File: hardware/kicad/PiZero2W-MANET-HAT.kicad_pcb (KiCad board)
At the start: 2 copper layers, 65 x 30 mm, 4 parts

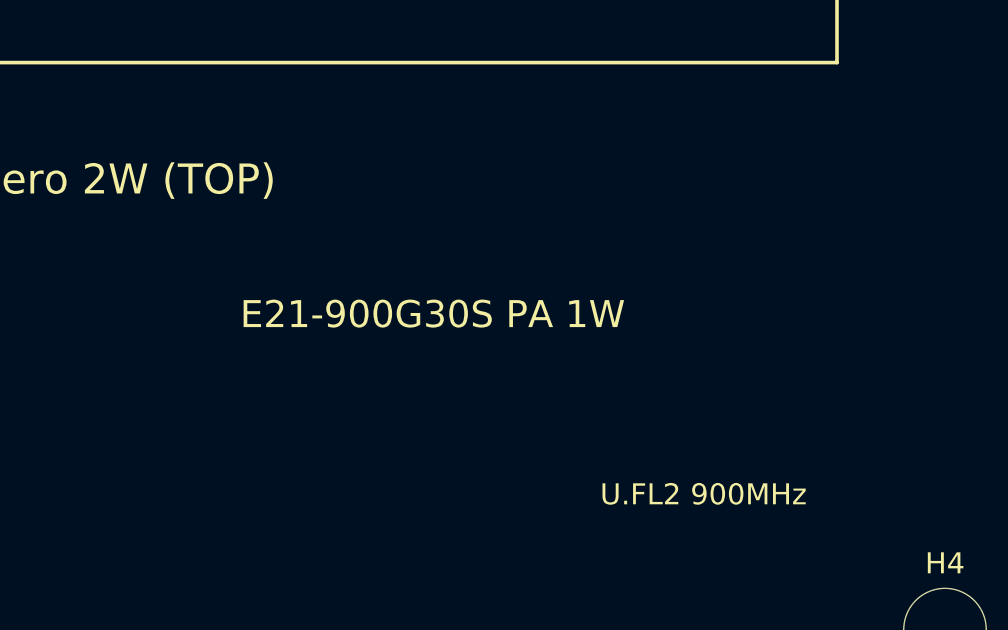
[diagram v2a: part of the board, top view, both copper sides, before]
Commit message: Make E21 PA a DNP/optional Variant B; default to module-only
Deployment is ground/handheld/vehicle (NLOS), where the E21's +3 dB buys
only ~20% range (LINK_BUDGET) against ~620 mA + heat + recert + RX-rate
risk. So restructure as one PCB with two BOM builds:

- Variant A (DEFAULT): module-only ~27 dBm via OpenMANET BCF. E21,
  buck-boost (VPA), LPF and drive pad are DNP; an RF bypass (C_BYP)
  carries the module ANT straight to U.FL #2. Low power (~0.35 A), good
  for battery handhelds, stays on the module's modular cert.
- Variant B (OPTIONAL): populate E21 + VPA + LPF + T/R for +30 dBm
  extended range (fixed/elevated LoS); remove C_BYP; needs custom-BCF
  FEM GPIO control + end-product recert. No respin required.

Updated DECISIONS (B5/B10 resolved + new §C variants & order), SCHEMATIC,
POWER (default-build budget), BOM (variant tags + C_BYP), netlist, README,
and regenerated the KiCad scaffold (bypass net + silk tags).

https://claude.ai/code/session_015nkkW85U3sPf5mcvrsMw7T
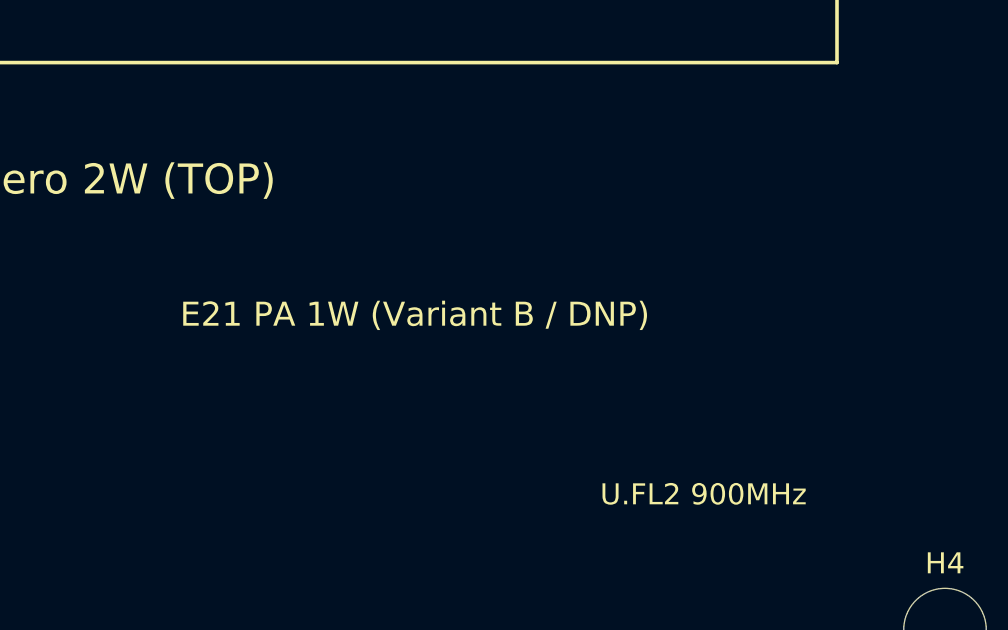
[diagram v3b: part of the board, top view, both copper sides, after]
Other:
- board text added: "E21 PA 1W (Variant B / DNP)"
- board text removed: "E21-900G30S PA 1W"
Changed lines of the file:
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@@
 	(gr_text "NEO-M9N" (at 10.5 16.0 0) (layer "F.SilkS") (effects (font (size 0.9 0.9) (thickness 0.12)) (justify left)))
 	(gr_text "U.FL1 GNSS" (at 2.0 22.0 0) (layer "F.SilkS") (effects (font (size 0.7 0.7) (thickness 0.12)) (justify left)))
-	(gr_text "E21-900G30S PA 1W" (at 38.0 16.0 0) (layer "F.SilkS") (effects (font (size 0.9 0.9) (thickness 0.12)) (justify left)))
+	(gr_text "E21 PA 1W (Variant B / DNP)" (at 36.0 16.0 0) (layer "F.SilkS") (effects (font (size 0.8 0.8) (thickness 0.12)) (justify left)))
 	(gr_text "U.FL2 900MHz" (at 50.0 22.0 0) (layer "F.SilkS") (effects (font (size 0.7 0.7) (thickness 0.12)) (justify left)))
 	(gr_text "4-layer recommended" (at 19.0 26.5 0) (layer "F.SilkS") (effects (font (size 0.7 0.7) (thickness 0.12)) (justify left)))

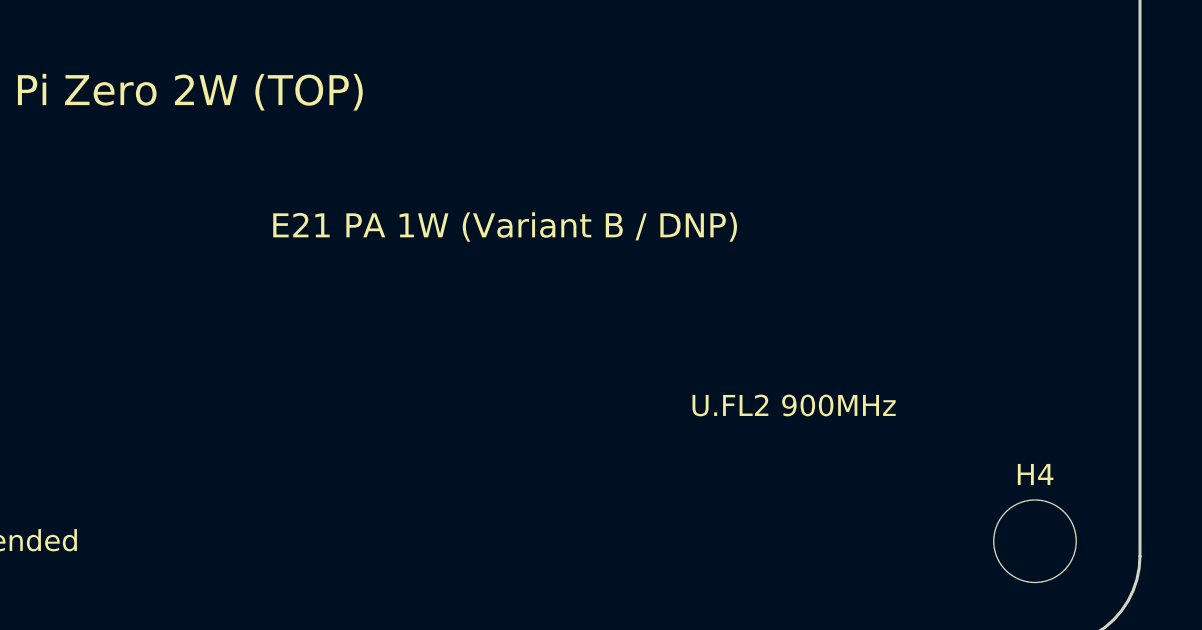
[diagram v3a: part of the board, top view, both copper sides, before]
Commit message: Pivot to MM8108-M20 primary / MF15457 fallback; retire external E21
Per the decision to make the MM8108-M20 the primary radio (with MF15457
as the build-today fallback) and retire the external E21 PA path:

Design:
- One radio site fed by the shared SPI/control nets accepts either module.
- Removed the E21 PA, 5V buck-boost (VPA), harmonic LPF, drive pad, T/R
  control, RF-sense VOX, and RF bypass. Both modules drive the antenna
  directly (M20 = integrated 28.5 dBm PA + 902-928 SAW, certified;
  MF15457 = ~27 dBm). Power collapses to a single 3V3 rail.
- Header GPIO4/6 (old FEM fallback) revert to spares; GPIO12/13 drive the
  status LEDs.
- M20 pinout/power/footprint held at placeholder pending its datasheet
  (B12); MF15457 pin-level detail stays the concrete baseline.

Docs updated: DECISIONS (A3 superseded, B11/B12 added, B2-B5/B10 retired,
new radio-options table + order), DESIGN, SCHEMATIC, POWER, RF, BOM,
INTERFACES, COMPONENTS_GAP, LINK_BUDGET, FIRMWARE_PA, BRINGUP, MECHANICAL,
README. Netlist, KiCad scaffold (sheets/silk/root note), and the OpenMANET
overlay/README updated to match. Scaffold regenerated and validated.

https://claude.ai/code/session_015nkkW85U3sPf5mcvrsMw7T
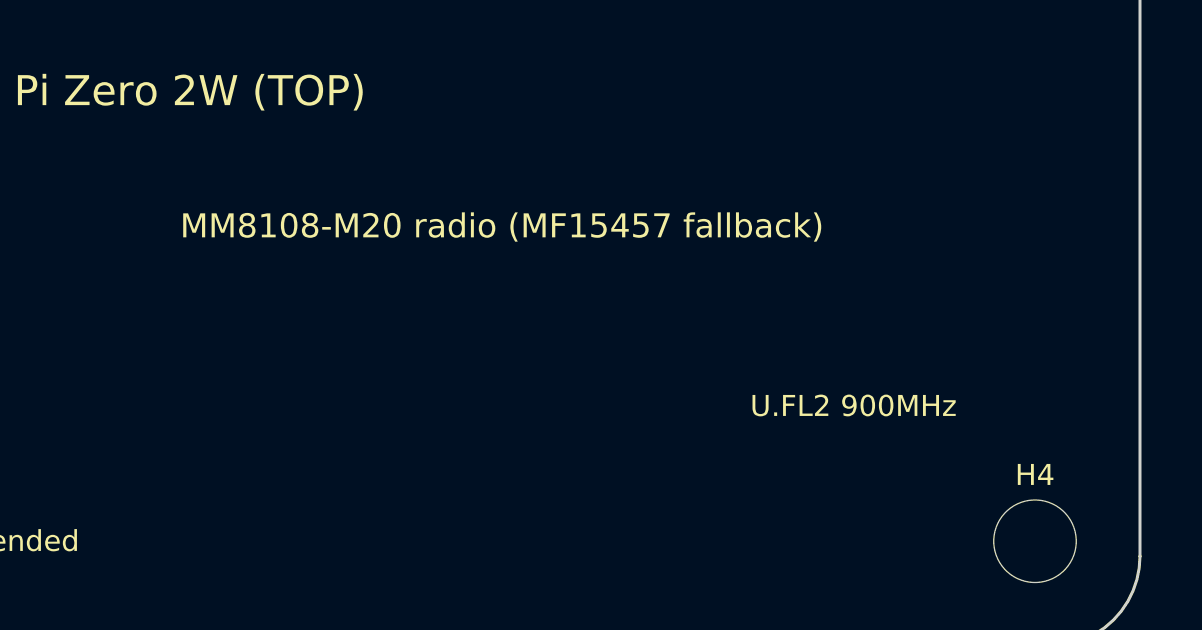
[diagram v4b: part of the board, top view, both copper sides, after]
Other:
- board text added: "3V3 BUCK + PWR MGMT (BTM)"
- board text added: "MM8108-M20 radio (MF15457 fallback)"
- board text added: "RTC + EEPROM (BTM)"
- board text removed: "BUCK-BOOST / 3V3 (BTM)"
- board text removed: "E21 PA 1W (Variant B / DNP)"
- board text removed: "EEPROM (BTM)"
- board text removed: "MM8108 + RF match (BTM)"
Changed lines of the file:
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@@
 	(gr_text "NEO-M9N" (at 10.5 16.0 0) (layer "F.SilkS") (effects (font (size 0.9 0.9) (thickness 0.12)) (justify left)))
 	(gr_text "U.FL1 GNSS" (at 2.0 22.0 0) (layer "F.SilkS") (effects (font (size 0.7 0.7) (thickness 0.12)) (justify left)))
-	(gr_text "E21 PA 1W (Variant B / DNP)" (at 36.0 16.0 0) (layer "F.SilkS") (effects (font (size 0.8 0.8) (thickness 0.12)) (justify left)))
-	(gr_text "U.FL2 900MHz" (at 50.0 22.0 0) (layer "F.SilkS") (effects (font (size 0.7 0.7) (thickness 0.12)) (justify left)))
+	(gr_text "MM8108-M20 radio (MF15457 fallback)" (at 33.0 16.0 0) (layer "F.SilkS") (effects (font (size 0.8 0.8) (thickness 0.12)) (justify left)))
+	(gr_text "U.FL2 900MHz" (at 52.0 22.0 0) (layer "F.SilkS") (effects (font (size 0.7 0.7) (thickness 0.12)) (justify left)))
 	(gr_text "4-layer recommended" (at 19.0 26.5 0) (layer "F.SilkS") (effects (font (size 0.7 0.7) (thickness 0.12)) (justify left)))
-	(gr_text "MM8108 + RF match (BTM)" (at 30.0 12.0 0) (layer "B.SilkS") (effects (font (size 0.9 0.9) (thickness 0.12)) (justify left mirror)))
-	(gr_text "BUCK-BOOST / 3V3 (BTM)" (at 30.0 18.0 0) (layer "B.SilkS") (effects (font (size 0.9 0.9) (thickness 0.12)) (justify left mirror)))
-	(gr_text "EEPROM (BTM)" (at 30.0 23.0 0) (layer "B.SilkS") (effects (font (size 0.8 0.8) (thickness 0.12)) (justify left mirror)))
+	(gr_text "3V3 BUCK + PWR MGMT (BTM)" (at 30.0 14.0 0) (layer "B.SilkS") (effects (font (size 0.9 0.9) (thickness 0.12)) (justify left mirror)))
+	(gr_text "RTC + EEPROM (BTM)" (at 30.0 20.0 0) (layer "B.SilkS") (effects (font (size 0.8 0.8) (thickness 0.12)) (justify left mirror)))
 	(gr_text "KEEPOUT: Pi HDMI/USB/SD/cam/RF-can" (at 30.0 26.5 0) (layer "B.SilkS") (effects (font (size 0.7 0.7) (thickness 0.12)) (justify left mirror)))
 )
